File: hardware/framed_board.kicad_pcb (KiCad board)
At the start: 2 copper layers, 110 x 40 mm, 106 parts, among them J1 Conn_ARM_JTAG_SWD_10, J2 USB_B_Micro, J3 Conn_01x04_Male, SW1 SW_Push, U1 LPC11U37FBD48-401_, U2 MCP1825S, Y1 Crystal

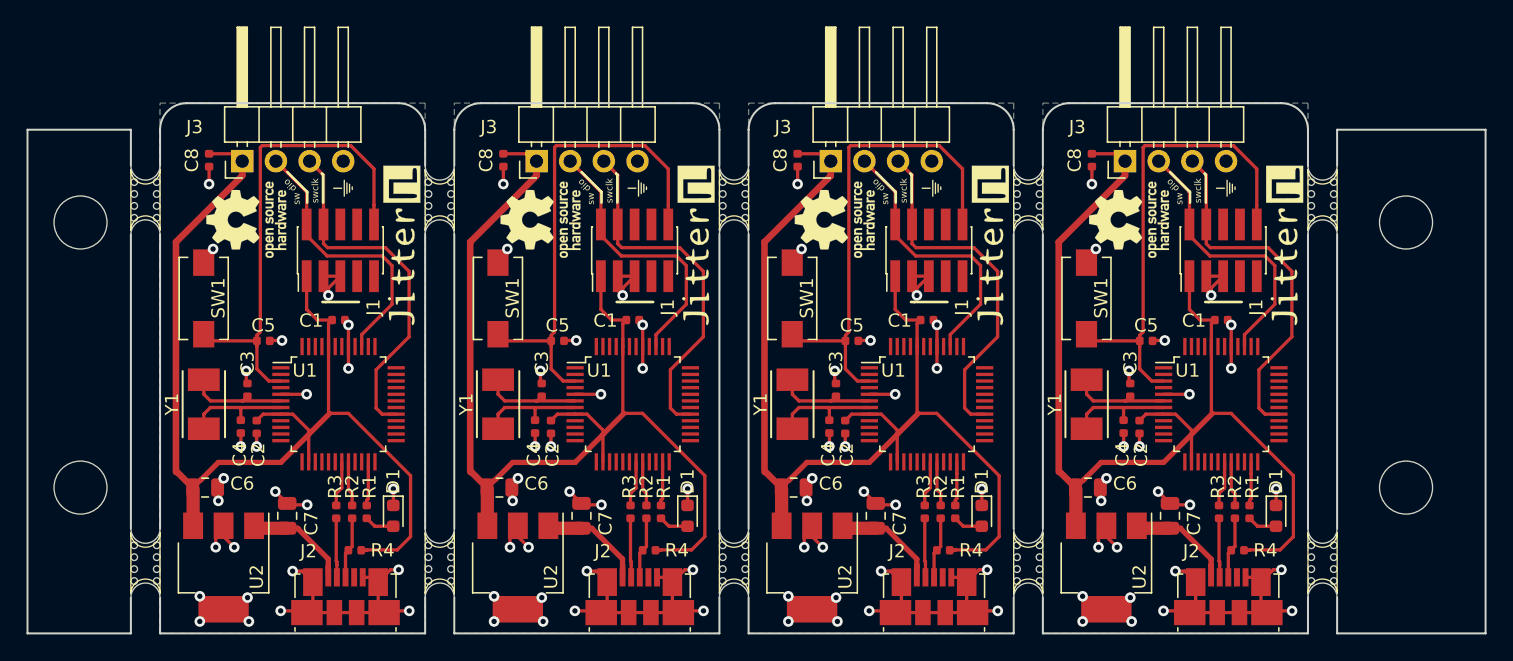
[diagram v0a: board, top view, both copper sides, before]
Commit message: Add frame with tooling holes and 4x LPC11 Blinkyboard.
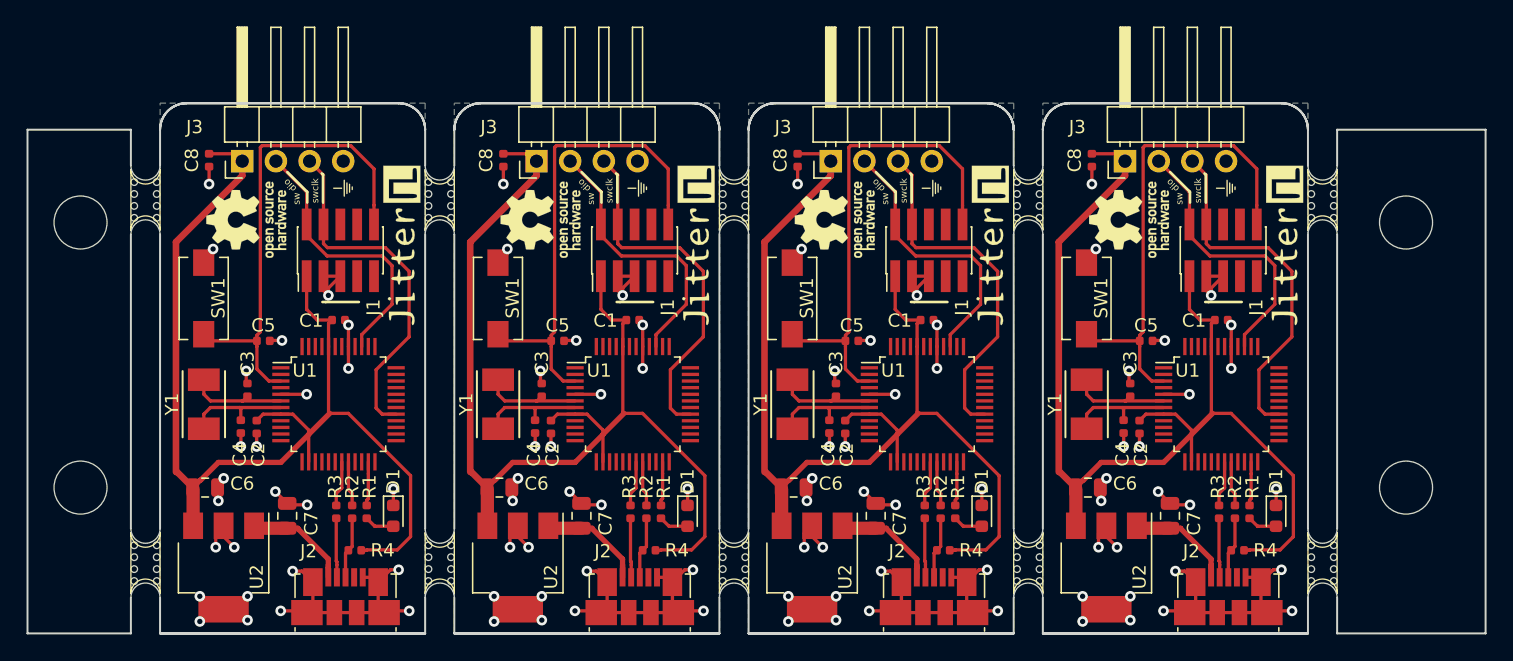
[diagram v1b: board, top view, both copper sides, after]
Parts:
- removed the G*** at (213.3, 149.7)
- removed the G*** at (191.1, 149.7)
- removed the G*** at (168.9, 149.7)
- removed the G*** at (146.7, 149.7)
- added G***: LOGO, Logo:Jitter-med, B.Cu at (213.3, 148.9)
- added G***: LOGO, Logo:Jitter-med, B.Cu at (191.1, 148.9)
- added G***: LOGO, Logo:Jitter-med, B.Cu at (168.9, 148.9)
- added G***: LOGO, Logo:Jitter-med, B.Cu at (146.7, 148.9)

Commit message: PCB layout: minor adjustments
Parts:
- removed the Y1 at (199.9, 142.7)
- removed the Y1 at (177.7, 142.7)
- removed the Y1 at (155.5, 142.7)
- removed the Y1 at (133.3, 142.7)
- added Y1: Crystal, Jitter_Footprints:Crystal_SMD_TXC_7A-2Pin_5.0x3.2mm, F.Cu at (199.9, 142.7)
- added Y1: Crystal, Jitter_Footprints:Crystal_SMD_TXC_7A-2Pin_5.0x3.2mm, F.Cu at (177.7, 142.7)
- added Y1: Crystal, Jitter_Footprints:Crystal_SMD_TXC_7A-2Pin_5.0x3.2mm, F.Cu at (155.5, 142.7)
- added Y1: Crystal, Jitter_Footprints:Crystal_SMD_TXC_7A-2Pin_5.0x3.2mm, F.Cu at (133.3, 142.7)
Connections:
- C1 pad 1: (no net) -> +3V3 (x4)
- C1 pad 2: (no net) -> GND (x4)
- C2 pad 1: (no net) -> +3V3 (x4)
- C2 pad 2: (no net) -> GND (x4)
- C3 pad 1: (no net) -> GND (x4)
- C3 pad 2: (no net) -> Net-(C3-Pad2) (x4)
- C4 pad 1: (no net) -> GND (x4)
- C4 pad 2: (no net) -> Net-(C4-Pad2) (x4)
- C5 pad 1: (no net) -> /RESET (x4)
- C5 pad 2: (no net) -> GND (x4)
- C6 pad 1: (no net) -> GND (x4)
- C6 pad 2: (no net) -> +3V3 (x4)
- C7 pad 1: (no net) -> GND (x4)
- C7 pad 2: (no net) -> +5V (x4)
- C8 pad 1: (no net) -> +3V3 (x4)
- C8 pad 2: (no net) -> GND (x4)
- D1 pad 1: (no net) -> GND (x4)
- D1 pad 2: (no net) -> Net-(D1-Pad2) (x4)
- J1 pad 1: (no net) -> +3V3 (x4)
- J1 pad 10: (no net) -> /RESET (x4)
- J1 pad 2: (no net) -> /SWDIO (x4)
- J1 pad 3: (no net) -> GND (x4)
- J1 pad 4: (no net) -> /SWCLK (x4)
- J1 pad 5: (no net) -> GND (x4)
- J1 pad 6: (no net) -> Net-(J1-Pad6) (x4)
- J1 pad 7: (no net) -> Net-(J1-Pad7) (x4)
- J1 pad 8: (no net) -> Net-(J1-Pad8) (x4)
- J1 pad 9: (no net) -> GND (x4)
- J2 pad 1: (no net) -> +5V (x4)
- J2 pad 2: (no net) -> /USBD- (x4)
- J2 pad 3: (no net) -> /USBD+ (x4)
- J2 pad 4: (no net) -> Net-(J2-Pad4) (x4)
- J2 pad 5: (no net) -> GND (x4)
- J2 pad 6: (no net) -> GND (x4)
- J3 pad 1: (no net) -> +3V3 (x4)
- J3 pad 2: (no net) -> /SWDIO (x4)
- J3 pad 3: (no net) -> /SWCLK (x4)
- J3 pad 4: (no net) -> GND (x4)
- R1 pad 1: (no net) -> Net-(R1-Pad1) (x4)
- R1 pad 2: (no net) -> Net-(D1-Pad2) (x4)
- R2 pad 1: (no net) -> /USBD+ (x4)
- R2 pad 2: (no net) -> Net-(R2-Pad2) (x4)
- R3 pad 1: (no net) -> /USBD- (x4)
- R3 pad 2: (no net) -> Net-(R3-Pad2) (x4)
- R4 pad 1: (no net) -> /USBD+ (x4)
- R4 pad 2: (no net) -> +3V3 (x4)
- SW1 pad 1: (no net) -> /RESET (x4)
- SW1 pad 2: (no net) -> GND (x4)
- U1 pad 1: (no net) -> Net-(U1-Pad1) (x4)
- U1 pad 10: (no net) -> Net-(U1-Pad10) (x4)
- U1 pad 11: (no net) -> Net-(U1-Pad11) (x4)
- U1 pad 12: (no net) -> Net-(U1-Pad12) (x4)
- U1 pad 13: (no net) -> Net-(U1-Pad13) (x4)
- U1 pad 14: (no net) -> +3V3 (x4)
- U1 pad 15: (no net) -> Net-(U1-Pad15) (x4)
- U1 pad 16: (no net) -> Net-(U1-Pad16) (x4)
- U1 pad 17: (no net) -> Net-(U1-Pad17) (x4)
- U1 pad 18: (no net) -> Net-(U1-Pad18) (x4)
- U1 pad 19: (no net) -> Net-(R3-Pad2) (x4)
- U1 pad 2: (no net) -> Net-(U1-Pad2) (x4)
- U1 pad 20: (no net) -> Net-(R2-Pad2) (x4)
- U1 pad 21: (no net) -> Net-(U1-Pad21) (x4)
- U1 pad 22: (no net) -> Net-(U1-Pad22) (x4)
- U1 pad 23: (no net) -> Net-(R1-Pad1) (x4)
- U1 pad 24: (no net) -> Net-(U1-Pad24) (x4)
- U1 pad 25: (no net) -> Net-(U1-Pad25) (x4)
- U1 pad 26: (no net) -> Net-(U1-Pad26) (x4)
- U1 pad 27: (no net) -> Net-(U1-Pad27) (x4)
- U1 pad 28: (no net) -> Net-(U1-Pad28) (x4)
- U1 pad 29: (no net) -> /SWCLK (x4)
- U1 pad 3: (no net) -> /RESET (x4)
- U1 pad 30: (no net) -> Net-(U1-Pad30) (x4)
- U1 pad 31: (no net) -> Net-(U1-Pad31) (x4)
- U1 pad 32: (no net) -> Net-(U1-Pad32) (x4)
- U1 pad 33: (no net) -> Net-(U1-Pad33) (x4)
- U1 pad 34: (no net) -> Net-(U1-Pad34) (x4)
- U1 pad 35: (no net) -> Net-(U1-Pad35) (x4)
- U1 pad 36: (no net) -> Net-(U1-Pad36) (x4)
- U1 pad 37: (no net) -> Net-(U1-Pad37) (x4)
- U1 pad 38: (no net) -> Net-(U1-Pad38) (x4)
- U1 pad 39: (no net) -> /SWDIO (x4)
- U1 pad 4: (no net) -> Net-(U1-Pad4) (x4)
- U1 pad 40: (no net) -> Net-(U1-Pad40) (x4)
- U1 pad 41: (no net) -> GND (x4)
- U1 pad 42: (no net) -> Net-(U1-Pad42) (x4)
- U1 pad 43: (no net) -> Net-(U1-Pad43) (x4)
- U1 pad 44: (no net) -> +3V3 (x4)
- U1 pad 45: (no net) -> Net-(U1-Pad45) (x4)
- U1 pad 46: (no net) -> Net-(U1-Pad46) (x4)
- U1 pad 47: (no net) -> Net-(U1-Pad47) (x4)
- U1 pad 48: (no net) -> Net-(U1-Pad48) (x4)
- U1 pad 5: (no net) -> GND (x4)
- U1 pad 6: (no net) -> Net-(C3-Pad2) (x4)
- U1 pad 7: (no net) -> Net-(C4-Pad2) (x4)
- U1 pad 8: (no net) -> +3V3 (x4)
- U1 pad 9: (no net) -> Net-(U1-Pad9) (x4)
- U2 pad 1: (no net) -> +5V (x4)
- U2 pad 2: (no net) -> GND (x4)
- U2 pad 3: (no net) -> +3V3 (x4)
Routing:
- net (no net): track 1036.3 -> 0.00 mm, vias 100 -> 0
- net +3V3: track 0.00 -> 331.0 mm
- net GND: track 0.00 -> 182.9 mm, vias 0 -> 108
- net /RESET: track 0.00 -> 154.8 mm
- net /SWCLK: track 0.00 -> 108.1 mm
- net /SWDIO: track 0.00 -> 88.7 mm
- net +5V: track 0.00 -> 35.9 mm
- net Net-(C4-Pad2): track 0.00 -> 32.5 mm
- net Net-(C3-Pad2): track 0.00 -> 30.6 mm
- net /USBD+: track 0.00 -> 18.6 mm
- net /USBD-: track 0.00 -> 17.9 mm
- net Net-(R3-Pad2): track 0.00 -> 13.8 mm
- net Net-(R2-Pad2): track 0.00 -> 13.6 mm
- net Net-(R1-Pad1): track 0.00 -> 13.3 mm
- net Net-(D1-Pad2): track 0.00 -> 9.04 mm
- added copper zone on B.Cu, net GND
- removed copper zone on B.Cu, net (none)
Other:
- outline, holes or cut-outs redrawn
- rule pad_to_mask_clearance: 0.2 -> 0.075
